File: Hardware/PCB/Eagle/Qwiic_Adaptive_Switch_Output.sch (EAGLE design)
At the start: 34 parts, among them J1 QWIIC_RIGHT_ANGLE, J4 QWIIC_RIGHT_ANGLE, SW1 CUI_SJ1-3513, SW2 CUI_SJ1-3513, U1 TCA9534

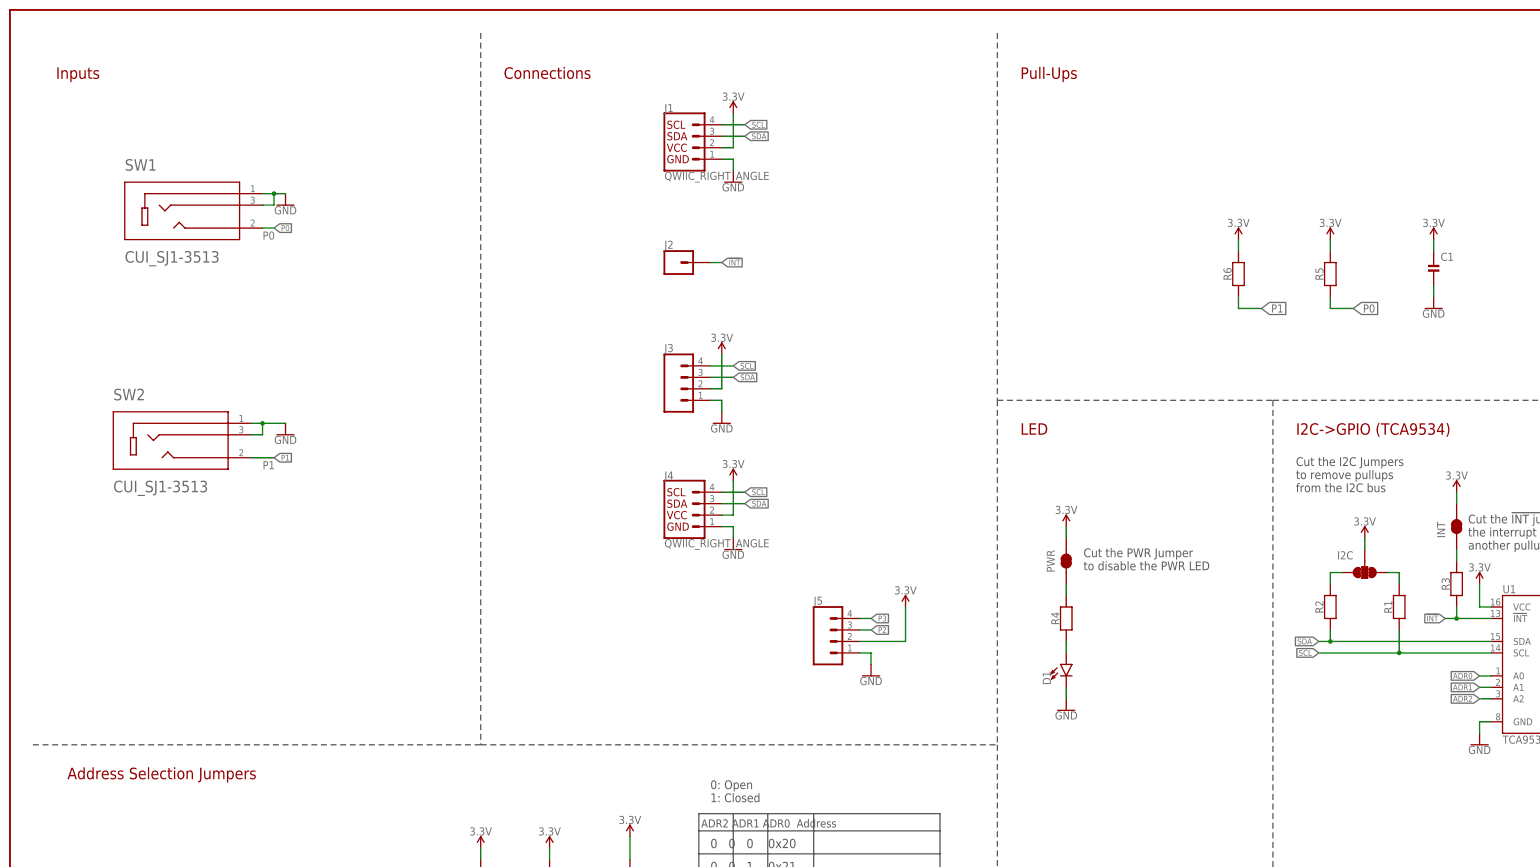
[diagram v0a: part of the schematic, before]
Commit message: Added Switch Output
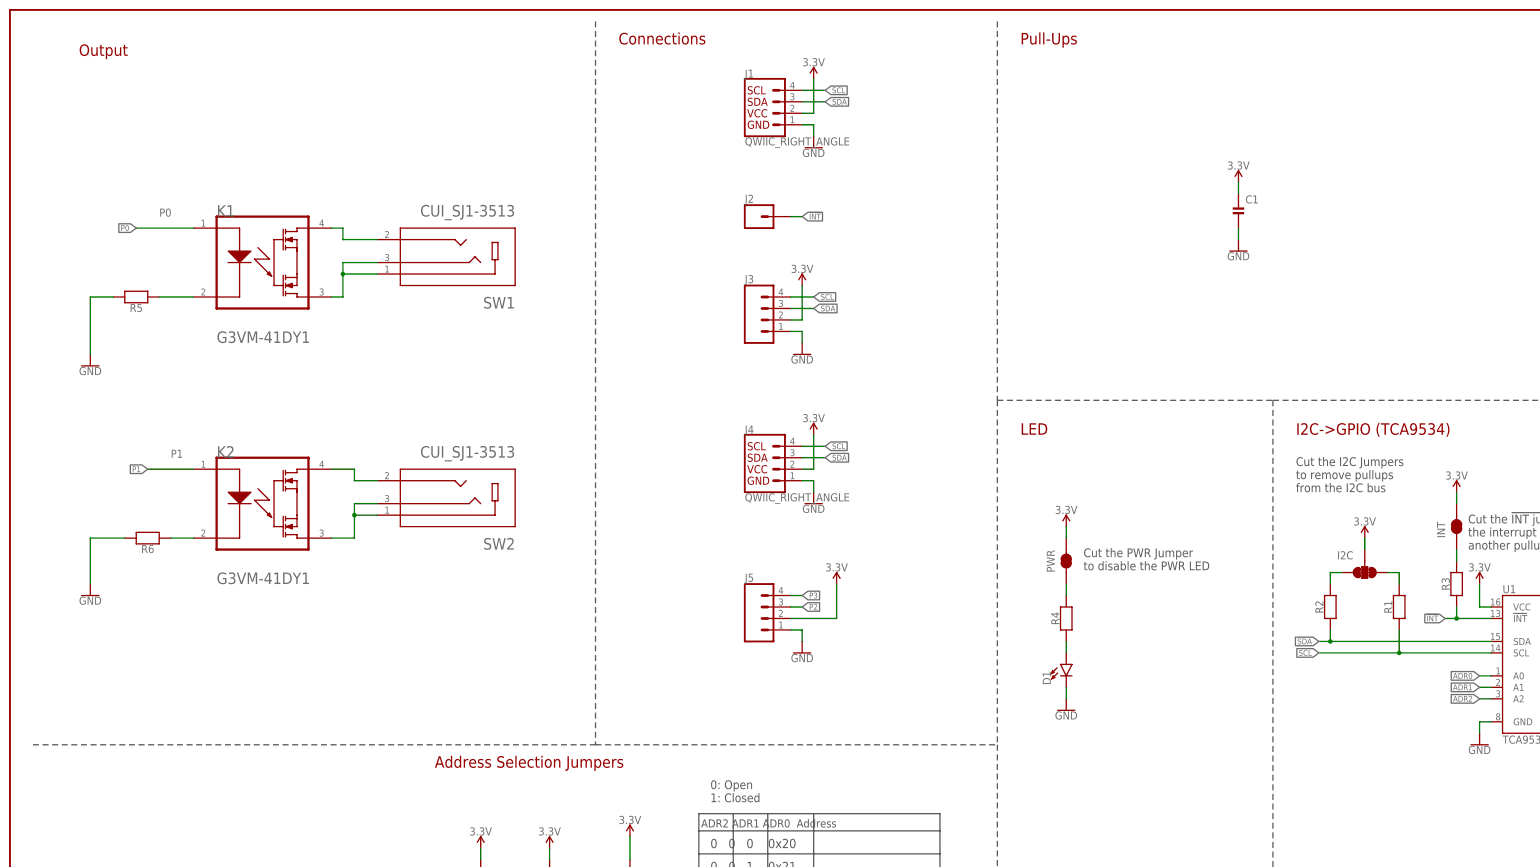
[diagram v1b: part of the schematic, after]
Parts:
- added K1, K2: G3VM-41DY1, milador_SMD:G3VM-41DY1
- LABEL_18, LABEL_9: value MILADOR-SWITCH-NAME-SW-INPUT -> MILADOR-SWITCH-NAME-SW-OUTPUT; device milador:MILADOR-SWITCH-NAME-SW-INPUT -> milador:MILADOR-SWITCH-NAME-SW-OUTPUT
- R5: value 4.7k -> 220
- R6: value 4.7K -> 220
- renumbered LABEL_14 to LABEL_13
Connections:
- new net N$4: K1.4, SW1.2
- new net N$5: K1.2, R5.1
- new net N$6: K1.3, SW1.1, SW1.3
- new net N$7: K2.2, R6.1
- new net N$8: K2.4, SW2.2
- new net N$9: K2.3, SW2.1, SW2.3
- net 3.3V: no longer R5.2, R6.2
- net GND: now also R5.2, R6.2; no longer SW1.1, SW1.3, SW2.1, SW2.3
- net P0: now also K1.1; no longer R5.1, SW1.2
- net P1: now also K2.1; no longer R6.1, SW2.2
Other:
- note added: "Output"
- note removed: "Inputs"
- moved on the sheet: C1, J1, J2, J3, J4, J5, R5, R6, SW1, SW2

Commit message: Updated PCB Mount holes
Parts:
- H1, H2: value STAND-OFF -> STAND-OFF-3.3; device SparkFun-Hardware:STAND-OFF -> milador:STAND-OFF-3.3
- JP3, JP4: value STAND-OFF -> STAND-OFF-3.3; device SparkFun:STAND-OFF -> milador:STAND-OFF-3.3
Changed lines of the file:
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@@
 </classes>
 <parts>
-<part name="JP3" library="SparkFun" deviceset="STAND-OFF" device=""/>
-<part name="JP4" library="SparkFun" deviceset="STAND-OFF" device=""/>
+<part name="JP3" library="milador" library_urn="urn:adsk.eagle:library:12595918" deviceset="STAND-OFF-" device="3.3" package3d_urn="urn:adsk.eagle:package:30775189/1"/>
+<part name="JP4" library="milador" library_urn="urn:adsk.eagle:library:12595918" deviceset="STAND-OFF-" device="3.3" package3d_urn="urn:adsk.eagle:package:30775189/1"/>
 <part name="SUPPLY4" library="SparkFun-PowerSymbols" deviceset="3.3V" device=""/>
 <part name="SUPPLY5" library="SparkFun-PowerSymbols" deviceset="3.3V" device=""/>
@@
 <part name="SUPPLY9" library="SparkFun-PowerSymbols" deviceset="3.3V" device=""/>
 <part name="I2C" library="milador_SMD" library_urn="urn:adsk.eagle:library:27847482" deviceset="JUMPERS_JUMPER-SMT_3_2-NC_TRACE" device="_SILK" package3d_urn="urn:adsk.eagle:package:29222217/1"/>
-<part name="H1" library="SparkFun-Hardware" deviceset="STAND-OFF" device=""/>
-<part name="H2" library="SparkFun-Hardware" deviceset="STAND-OFF" device=""/>
+<part name="H1" library="milador" library_urn="urn:adsk.eagle:library:12595918" deviceset="STAND-OFF-" device="3.3" package3d_urn="urn:adsk.eagle:package:30775189/1"/>
+<part name="H2" library="milador" library_urn="urn:adsk.eagle:library:12595918" deviceset="STAND-OFF-" device="3.3" package3d_urn="urn:adsk.eagle:package:30775189/1"/>
 <part name="R3" library="milador_SMD" library_urn="urn:adsk.eagle:library:27847482" deviceset="RESISTOR-" device="0603" package3d_urn="urn:adsk.eagle:package:29222124/2" value="10k"/>
 <part name="SUPPLY12" library="SparkFun-PowerSymbols" deviceset="3.3V" device=""/>

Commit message: Updated footprints to 0805 packages
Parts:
- C1: device milador_SMD:CAP_CERAMIC-0603 -> milador_SMD:CAP_CERAMIC-0805-MP
- R1, R2, R3, R4, R5, R6, R7, R8, R9: device milador_SMD:RESISTOR-0603 -> milador_SMD:RESISTOR-0805-MP
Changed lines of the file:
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@@
 </part>
 <part name="SUPPLY7" library="SparkFun-PowerSymbols" deviceset="3.3V" device=""/>
-<part name="C1" library="milador_SMD" library_urn="urn:adsk.eagle:library:27847482" deviceset="CAP_CERAMIC-" device="0603" package3d_urn="urn:adsk.eagle:package:29222124/2" value="0.1uF"/>
+<part name="C1" library="milador_SMD" library_urn="urn:adsk.eagle:library:27847482" deviceset="CAP_CERAMIC-" device="0805-MP" package3d_urn="urn:adsk.eagle:package:27847629/3" value="0.1uF"/>
 <part name="SUPPLY8" library="SparkFun-PowerSymbols" deviceset="3.3V" device=""/>
 <part name="J4" library="milador_SMD" library_urn="urn:adsk.eagle:library:27847482" deviceset="QWIIC_CONNECTORS" device="JS-1MM" package3d_urn="urn:adsk.eagle:package:29222212/3" value="QWIIC_RIGHT_ANGLE">
 <attribute name="PROD_ID" value="CONN-13694"/>
 </part>
-<part name="R2" library="milador_SMD" library_urn="urn:adsk.eagle:library:27847482" deviceset="RESISTOR-" device="0603" package3d_urn="urn:adsk.eagle:package:29222124/2" value="2.2k"/>
-<part name="R1" library="milador_SMD" library_urn="urn:adsk.eagle:library:27847482" deviceset="RESISTOR-" device="0603" package3d_urn="urn:adsk.eagle:package:29222124/2" value="2.2k"/>
+<part name="R2" library="milador_SMD" library_urn="urn:adsk.eagle:library:27847482" deviceset="RESISTOR-" device="0805-MP" package3d_urn="urn:adsk.eagle:package:27847629/3" value="2.2k"/>
+<part name="R1" library="milador_SMD" library_urn="urn:adsk.eagle:library:27847482" deviceset="RESISTOR-" device="0805-MP" package3d_urn="urn:adsk.eagle:package:27847629/3" value="2.2k"/>
 <part name="SUPPLY1" library="SparkFun-PowerSymbols" deviceset="3.3V" device=""/>
 <part name="U1" library="milador_SMD" library_urn="urn:adsk.eagle:library:27847482" deviceset="TCA9534" device="U" package3d_urn="urn:adsk.eagle:package:29222127/2" value="TCA9534"/>
-<part name="R7" library="milador_SMD" library_urn="urn:adsk.eagle:library:27847482" deviceset="RESISTOR-" device="0603" package3d_urn="urn:adsk.eagle:package:29222124/2" value="2.2k"/>
-<part name="R8" library="milador_SMD" library_urn="urn:adsk.eagle:library:27847482" deviceset="RESISTOR-" device="0603" package3d_urn="urn:adsk.eagle:package:29222124/2" value="2.2k"/>
-<part name="R9" library="milador_SMD" library_urn="urn:adsk.eagle:library:27847482" deviceset="RESISTOR-" device="0603" package3d_urn="urn:adsk.eagle:package:29222124/2" value="2.2k"/>
+<part name="R7" library="milador_SMD" library_urn="urn:adsk.eagle:library:27847482" deviceset="RESISTOR-" device="0805-MP" package3d_urn="urn:adsk.eagle:package:27847629/3" value="2.2k"/>
+<part name="R8" library="milador_SMD" library_urn="urn:adsk.eagle:library:27847482" deviceset="RESISTOR-" device="0805-MP" package3d_urn="urn:adsk.eagle:package:27847629/3" value="2.2k"/>
+<part name="R9" library="milador_SMD" library_urn="urn:adsk.eagle:library:27847482" deviceset="RESISTOR-" device="0805-MP" package3d_urn="urn:adsk.eagle:package:27847629/3" value="2.2k"/>
 <part name="SUPPLY2" library="SparkFun-PowerSymbols" deviceset="3.3V" device=""/>
 <part name="SUPPLY3" library="SparkFun-PowerSymbols" deviceset="3.3V" device=""/>
@@
 <part name="H1" library="milador" library_urn="urn:adsk.eagle:library:12595918" deviceset="STAND-OFF-" device="3.3" package3d_urn="urn:adsk.eagle:package:30775189/1"/>
 <part name="H2" library="milador" library_urn="urn:adsk.eagle:library:12595918" deviceset="STAND-OFF-" device="3.3" package3d_urn="urn:adsk.eagle:package:30775189/1"/>
-<part name="R3" library="milador_SMD" library_urn="urn:adsk.eagle:library:27847482" deviceset="RESISTOR-" device="0603" package3d_urn="urn:adsk.eagle:package:29222124/2" value="10k"/>
+<part name="R3" library="milador_SMD" library_urn="urn:adsk.eagle:library:27847482" deviceset="RESISTOR-" device="0805-MP" package3d_urn="urn:adsk.eagle:package:27847629/3" value="10k"/>
 <part name="SUPPLY12" library="SparkFun-PowerSymbols" deviceset="3.3V" device=""/>
 <part name="INT" library="milador_SMD" library_urn="urn:adsk.eagle:library:27847482" deviceset="JUMPERS-SMT_2_NC_TRACE" device="_SILK" package3d_urn="urn:adsk.eagle:package:29222215/1"/>
@@
 <part name="SUPPLY13" library="SparkFun-PowerSymbols" deviceset="3.3V" device=""/>
 <part name="PWR" library="milador_SMD" library_urn="urn:adsk.eagle:library:27847482" deviceset="JUMPERS-SMT_2_NC_TRACE" device="_SILK" package3d_urn="urn:adsk.eagle:package:29222215/1"/>
-<part name="R4" library="milador_SMD" library_urn="urn:adsk.eagle:library:27847482" deviceset="RESISTOR-" device="0603" package3d_urn="urn:adsk.eagle:package:29222124/2" value="1k"/>
+<part name="R4" library="milador_SMD" library_urn="urn:adsk.eagle:library:27847482" deviceset="RESISTOR-" device="0805-MP" package3d_urn="urn:adsk.eagle:package:27847629/3" value="1k"/>
 <part name="D1" library="milador_SMD" library_urn="urn:adsk.eagle:library:27847482" deviceset="LED" device="" package3d_urn="urn:adsk.eagle:package:29222125/2" value="RED"/>
 <part name="GND8" library="SparkFun-PowerSymbols" deviceset="GND" device=""/>
@@
 <part name="GND10" library="SparkFun-PowerSymbols" deviceset="GND" device=""/>
 <part name="GND14" library="SparkFun-PowerSymbols" deviceset="GND" device=""/>
-<part name="R5" library="milador_SMD" library_urn="urn:adsk.eagle:library:27847482" deviceset="RESISTOR-" device="0603" package3d_urn="urn:adsk.eagle:package:29222124/2" value="220"/>
-<part name="R6" library="milador_SMD" library_urn="urn:adsk.eagle:library:27847482" deviceset="RESISTOR-" device="0603" package3d_urn="urn:adsk.eagle:package:29222124/2" value="220"/>
+<part name="R5" library="milador_SMD" library_urn="urn:adsk.eagle:library:27847482" deviceset="RESISTOR-" device="0805-MP" package3d_urn="urn:adsk.eagle:package:27847629/3" value="220"/>
+<part name="R6" library="milador_SMD" library_urn="urn:adsk.eagle:library:27847482" deviceset="RESISTOR-" device="0805-MP" package3d_urn="urn:adsk.eagle:package:27847629/3" value="220"/>
 </parts>
 <sheets>

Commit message: Updated silkscreen
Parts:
- D1: device milador_SMD:LED -> milador_SMD:LED0805_NOOUTLINE
- U1: device milador_SMD:TCA9534U -> milador_SMD:TCA9534DWR
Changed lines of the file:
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@@
 <part name="R1" library="milador_SMD" library_urn="urn:adsk.eagle:library:27847482" deviceset="RESISTOR-" device="0805-MP" package3d_urn="urn:adsk.eagle:package:27847629/3" value="2.2k"/>
 <part name="SUPPLY1" library="SparkFun-PowerSymbols" deviceset="3.3V" device=""/>
-<part name="U1" library="milador_SMD" library_urn="urn:adsk.eagle:library:27847482" deviceset="TCA9534" device="U" package3d_urn="urn:adsk.eagle:package:29222127/2" value="TCA9534"/>
+<part name="U1" library="milador_SMD" library_urn="urn:adsk.eagle:library:27847482" deviceset="TCA9534" device="DWR" package3d_urn="urn:adsk.eagle:package:29222127/2" value="TCA9534"/>
 <part name="R7" library="milador_SMD" library_urn="urn:adsk.eagle:library:27847482" deviceset="RESISTOR-" device="0805-MP" package3d_urn="urn:adsk.eagle:package:27847629/3" value="2.2k"/>
 <part name="R8" library="milador_SMD" library_urn="urn:adsk.eagle:library:27847482" deviceset="RESISTOR-" device="0805-MP" package3d_urn="urn:adsk.eagle:package:27847629/3" value="2.2k"/>
@@
 <part name="PWR" library="milador_SMD" library_urn="urn:adsk.eagle:library:27847482" deviceset="JUMPERS-SMT_2_NC_TRACE" device="_SILK" package3d_urn="urn:adsk.eagle:package:29222215/1"/>
 <part name="R4" library="milador_SMD" library_urn="urn:adsk.eagle:library:27847482" deviceset="RESISTOR-" device="0805-MP" package3d_urn="urn:adsk.eagle:package:27847629/3" value="1k"/>
-<part name="D1" library="milador_SMD" library_urn="urn:adsk.eagle:library:27847482" deviceset="LED" device="" package3d_urn="urn:adsk.eagle:package:29222125/2" value="RED"/>
+<part name="D1" library="milador_SMD" library_urn="urn:adsk.eagle:library:27847482" deviceset="LED" device="0805_NOOUTLINE" package3d_urn="urn:adsk.eagle:package:30853605/2" value="RED"/>
 <part name="GND8" library="SparkFun-PowerSymbols" deviceset="GND" device=""/>
 <part name="J2" library="milador" library_urn="urn:adsk.eagle:library:12595918" deviceset="CONNECTORS_CONN_01" device="PTH_NO_SILK_YES_STOP" package3d_urn="urn:adsk.eagle:package:29222250/2"/>
@@
 <part name="LABEL_18" library="milador" library_urn="urn:adsk.eagle:library:12595918" deviceset="MILADOR-SWITCH-NAME-" device="SW-OUTPUT" package3d_urn="urn:adsk.eagle:package:30678308/1" value="MILADOR-SWITCH-NAME-SW-OUTPUT"/>
 <part name="LABEL_9" library="milador" library_urn="urn:adsk.eagle:library:12595918" deviceset="MILADOR-SWITCH-NAME-" device="SW-OUTPUT" package3d_urn="urn:adsk.eagle:package:30678308/1" value="MILADOR-SWITCH-NAME-SW-OUTPUT"/>
-<part name="K1" library="milador_SMD" library_urn="urn:adsk.eagle:library:27847482" deviceset="G3VM-41DY1" device="" package3d_urn="urn:adsk.eagle:package:30688509/2"/>
-<part name="K2" library="milador_SMD" library_urn="urn:adsk.eagle:library:27847482" deviceset="G3VM-41DY1" device="" package3d_urn="urn:adsk.eagle:package:30688509/2"/>
+<part name="K1" library="milador_SMD" library_urn="urn:adsk.eagle:library:27847482" deviceset="G3VM-41DY1" device="" package3d_urn="urn:adsk.eagle:package:30688509/3"/>
+<part name="K2" library="milador_SMD" library_urn="urn:adsk.eagle:library:27847482" deviceset="G3VM-41DY1" device="" package3d_urn="urn:adsk.eagle:package:30688509/3"/>
 <part name="GND10" library="SparkFun-PowerSymbols" deviceset="GND" device=""/>
 <part name="GND14" library="SparkFun-PowerSymbols" deviceset="GND" device=""/>

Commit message: Updated design to version 1.2
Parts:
- removed J4: QWIIC_RIGHT_ANGLE, milador_SMD:QWIIC_CONNECTORSJS-1MM
- removed J5: (no value), milador:CONNECTORS_CONN_041X04_NO_SILK
- removed LABEL_13: MILADOR-LOGO-, milador:MILADOR-LOGO-
- removed LABEL_18, LABEL_9: MILADOR-SWITCH-NAME-SW-OUTPUT, milador:MILADOR-SWITCH-NAME-SW-OUTPUT
- removed LABEL_2: MILADOR-SWITCH-NAME-SW1, milador:MILADOR-SWITCH-NAME-SW1
- removed LABEL_3: MILADOR-SWITCH-NAME-SW2, milador:MILADOR-SWITCH-NAME-SW2
- added LABEL_!INT_BOTTOM, LABEL_!INT_TOP: MILADOR-LABEL-!INT, milador:MILADOR-LABEL-!INT
- added LABEL_3V_BOTTOM, LABEL_3V_TOP: MILADOR-LABEL-3V, milador:MILADOR-LABEL-3V
- added LABEL_ADR0: MILADOR-LABEL-ADR0, milador:MILADOR-LABEL-ADR0
- added LABEL_ADR1: MILADOR-LABEL-ADR1, milador:MILADOR-LABEL-ADR1
- added LABEL_ADR2: MILADOR-LABEL-ADR2, milador:MILADOR-LABEL-ADR2
- added LABEL_GND_BOTTOM, LABEL_GND_TOP: MILADOR-LABEL-GND, milador:MILADOR-LABEL-GND
- added LABEL_I2C: MILADOR-LABEL-I2C, milador:MILADOR-LABEL-I2C
- added LABEL_I2C_ADDRESS: MILADOR-LABEL-ADDRESS-0X27, milador:MILADOR-LABEL-ADDRESS-0X27
- added LABEL_INT: MILADOR-LABEL-INT, milador:MILADOR-LABEL-INT
- added LABEL_MILADOR_BOTTOM, LABEL_MILADOR_TOP: MILADOR-LOGO-, milador:MILADOR-LOGO-
- added LABEL_OUTPUT_BOTTOM, LABEL_OUTPUT_TOP: MILADOR-SWITCH-NAME-SW-OUTPUT, milador:MILADOR-SWITCH-NAME-SW-OUTPUT
- added LABEL_P0_BOTTOM: MILADOR-LABEL-P0, milador:MILADOR-LABEL-P0
- added LABEL_P1_BOTTOM: MILADOR-LABEL-P1, milador:MILADOR-LABEL-P1
- added LABEL_P2_BOTTOM, LABEL_P2_TOP: MILADOR-LABEL-P2, milador:MILADOR-LABEL-P2
- added LABEL_P3_BOTTOM, LABEL_P3_TOP: MILADOR-LABEL-P3, milador:MILADOR-LABEL-P3
- added LABEL_PWR: MILADOR-LABEL-PWR, milador:MILADOR-LABEL-PWR
- added LABEL_SW1: MILADOR-SWITCH-NAME-SW1, milador:MILADOR-SWITCH-NAME-SW1
- added LABEL_SW2: MILADOR-SWITCH-NAME-SW2, milador:MILADOR-SWITCH-NAME-SW2
- added LABEL_TITLE_BOTTOM: MILADOR-DEVICE-QWIIC-SWITCH, milador:MILADOR-DEVICE-QWIIC-SWITCH
- added LABEL_TITLE_TOP: MILADOR-DEVICE-QWIIC-SWITCH-SM, milador:MILADOR-DEVICE-QWIIC-SWITCH-SM
- added LABE_SCL_BOTTOM, LABE_SCL_TOP: MILADOR-LABEL-SCL, milador:MILADOR-LABEL-SCL
- added LABE_SDA_BOTTOM, LABE_SDA_TOP: MILADOR-LABEL-SDA, milador:MILADOR-LABEL-SDA
- J2: device milador:CONNECTORS_CONN_01PTH_NO_SILK_YES_STOP -> milador:CONNECTORS_CONN_071X07_NO_SILK
- J3: value (none) -> QWIIC_RIGHT_ANGLE; device milador:CONNECTORS_CONN_041X04_NO_SILK -> milador_SMD:QWIIC_CONNECTORSJS-1MM; PROD_ID (none) -> CONN-13694
- R3: value 10k -> 1k
- R4: value 1k -> 2.2k
- R5, R6: value 220 -> 2.2k
- R7, R8: value 2.2k -> 220
- R9: value 2.2k -> 10k
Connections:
- net !INT: now also J2.7, R9.1; no longer J2.1, R3.1
- net 3.3V: now also J2.1; no longer J4.2, J5.2
- net ADR0: now also R6.2; no longer R9.2
- net ADR1: now also R5.2; no longer R8.2
- net ADR2: now also R4.2; no longer R7.2
- net GND: now also J2.2, R4.1, R5.1, R6.1, R7.2, R8.2; no longer J4.1, J5.1, R5.2, R6.2, R7.1, R8.1, R9.1
- net N$1: now also R9.2; no longer R3.2
- net N$2: now also R3.1; no longer R4.1
- net N$3: now also R3.2; no longer R4.2
- net N$5: now also R7.1; no longer R5.1
- net N$7: now also R8.1; no longer R6.1
- net P2: now also J2.5; no longer J5.3
- net P3: now also J2.6; no longer J5.4
- net SCL: now also J2.3, R2.1; no longer J4.4, R1.1
- net SCL_PU1: now also R1.2; no longer R2.2
- net SDA: now also J2.4, R1.1; no longer J4.3, R2.1
- net SDA_PU1: now also R2.2; no longer R1.2
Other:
- moved on the sheet: ADR0, ADR1, ADR2, C1, R1, R2, R3, R4, R5, R6, R7, R8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
